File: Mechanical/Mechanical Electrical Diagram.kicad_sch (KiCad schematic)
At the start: 2 parts, among them U1 L298N

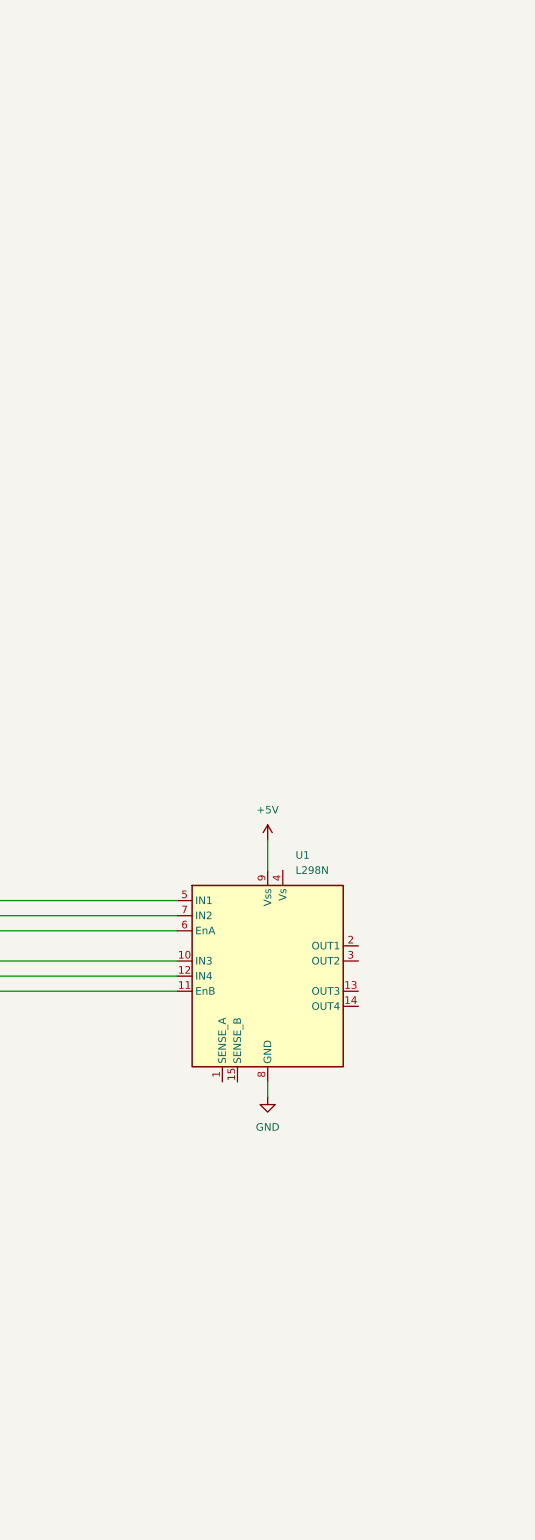
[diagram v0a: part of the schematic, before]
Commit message: Created Symbol Library
- Includes Jetson Nano
- Added Motor Controllers
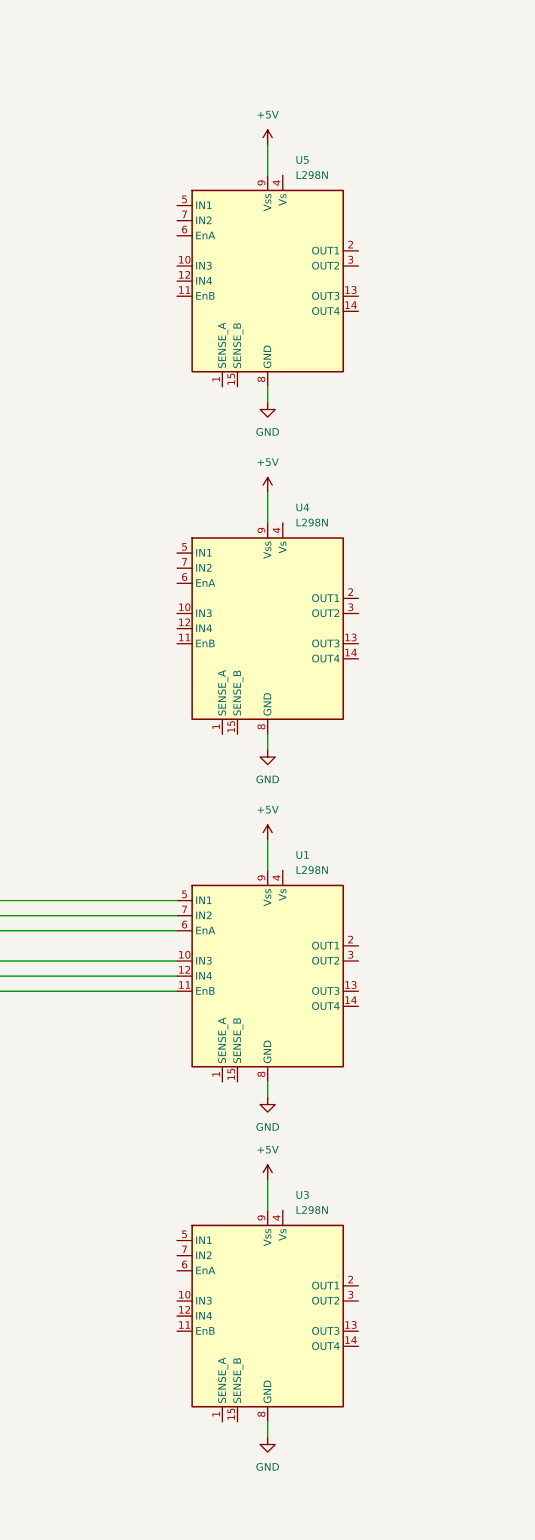
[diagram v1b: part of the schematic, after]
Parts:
- added U3, U4, U5: L298N, Package_TO_SOT_THT:TO-220-15_P2.54x5.08mm_StaggerOdd_Lead4.58mm_Vertical, symbol Driver_Motor:L298N
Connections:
- net +5V: now also U3.9 (Vss), U4.9 (Vss), U5.9 (Vss)
- net GND: now also U3.8 (GND), U4.8 (GND), U5.8 (GND)

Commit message: Updated Mechanical Wiring Diagram
- Removed Jetson Nano
- Added 4 Motor Controllers
- Added 4 Motors
- Waiting on Updated Symbol for Motors
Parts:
- removed U2: ~, symbol Jetson Nano:Jetson_Nano
- removed U4: L298N, Package_TO_SOT_THT:TO-220-15_P2.54x5.08mm_StaggerOdd_Lead4.58mm_Vertical, symbol Driver_Motor:L298N
- added M1, M2, M3, M4: Motor_DC, symbol Motor:Motor_DC
- added U2: L298N, Package_TO_SOT_THT:TO-220-15_P2.54x5.08mm_StaggerOdd_Lead4.58mm_Vertical, symbol Driver_Motor:L298N
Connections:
- net +5V: now also U2.9 (Vss)
- net GND: now also U2.8 (GND)
- net at U5.13 (OUT3): now also M1.1 (+)
- net at U5.14 (OUT4): now also M1.2 (-)
- net at U3.13 (OUT3): now also M4.1 (+)
- net at U3.14 (OUT4): now also M4.2 (-)
- net at U1.13 (OUT3): now also M2.1 (+)
- net at U1.14 (OUT4): now also M2.2 (-)
- new net: M3.1 (+), U2.13 (OUT3)
- new net: M3.2 (-), U2.14 (OUT4)
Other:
- moved on the sheet: U5

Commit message: Added notes to schematics
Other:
- note added: "Looks good, we'll just sub in the actual motor schematic from the library."
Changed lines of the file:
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@@
 	(generator_version "9.0")
 	(paper "A2")
+	(text "Looks good, we'll just sub in the actual motor schematic from the library. "
+		(exclude_from_sim no)
+		(at 206.756 218.694 0)
+		(effects
+			(font
+				(size 1.27 1.27)
+			)
+		)
+	)
 	(wire
 		(pts

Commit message: Fixed Sparkmax
I forgor that the encoder cable was separate from the white cable. Fixed it.
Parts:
- removed M1, M2, M3, M4: Motor_DC, symbol Motor:Motor_DC
- removed U1, U2, U3, U5: L298N, Package_TO_SOT_THT:TO-220-15_P2.54x5.08mm_StaggerOdd_Lead4.58mm_Vertical, symbol Driver_Motor:L298N
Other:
- note removed: "Looks good, we'll just sub in the actual motor schematic from the library."

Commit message: Updated Mechanical Diagram
Installed 5 Neo Motors and SparkMax Controllers
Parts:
- added U1, U10, U11, U12, U15, U17, U19, U2, U21, U3, U4, U5, U6, U7, U8, U9: ~, symbol Lunabotics 2025-26:Spark_Max_Motor_Controller
- added U13, U14, U16, U18, U20: ~, symbol Lunabotics 2025-26:Rev_Neo
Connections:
- new net: U11.1 (M+_(Red)), U19.1 (M+_(Red)), U6.1 (M+_(Red)), U7.1 (M+_(Red))
- new net: U11.2 (M-_(Black)), U18.1 (M+), U19.2 (M-_(Black)), U6.2 (M-_(Black)), U7.2 (M-_(Black))
- new net: U11.3 (Brushless_(White)), U18.3 (C), U19.3 (Brushless_(White)), U6.3 (Brushless_(White)), U7.3 (Brushless_(White))
- new net: U11.9 (Encoder_Sensor_(6Pin)), U18.4 (Enc_Cable), U19.9 (Encoder_Sensor_(6Pin)), U6.9 (Encoder_Sensor_(6Pin)), U7.9 (Encoder_Sensor_(6Pin))
- new net: U10.2 (M-_(Black)), U16.1 (M+), U17.2 (M-_(Black)), U4.2 (M-_(Black)), U5.2 (M-_(Black))
- new net: U10.3 (Brushless_(White)), U16.3 (C), U17.3 (Brushless_(White)), U4.3 (Brushless_(White)), U5.3 (Brushless_(White))
- new net: U10.9 (Encoder_Sensor_(6Pin)), U16.4 (Enc_Cable), U17.9 (Encoder_Sensor_(6Pin)), U4.9 (Encoder_Sensor_(6Pin)), U5.9 (Encoder_Sensor_(6Pin))
- new net: U14.1 (M+), U15.2 (M-_(Black)), U2.2 (M-_(Black)), U3.2 (M-_(Black)), U9.2 (M-_(Black))
- new net: U14.3 (C), U15.3 (Brushless_(White)), U2.3 (Brushless_(White)), U3.3 (Brushless_(White)), U9.3 (Brushless_(White))
- new net: U14.4 (Enc_Cable), U15.9 (Encoder_Sensor_(6Pin)), U2.9 (Encoder_Sensor_(6Pin)), U3.9 (Encoder_Sensor_(6Pin)), U9.9 (Encoder_Sensor_(6Pin))
- new net: U15.1 (M+_(Red)), U2.1 (M+_(Red)), U3.1 (M+_(Red)), U9.1 (M+_(Red))
- new net: U12.1 (M+_(Red)), U21.1 (M+_(Red)), U8.1 (M+_(Red))
- new net: U12.2 (M-_(Black)), U20.1 (M+), U21.2 (M-_(Black)), U8.2 (M-_(Black))
- new net: U12.3 (Brushless_(White)), U20.3 (C), U21.3 (Brushless_(White)), U8.3 (Brushless_(White))
- new net: U12.9 (Encoder_Sensor_(6Pin)), U20.4 (Enc_Cable), U21.9 (Encoder_Sensor_(6Pin)), U8.9 (Encoder_Sensor_(6Pin))
- new net: U10.1 (M+_(Red)), U17.1 (M+_(Red)), U4.1 (M+_(Red)), U5.1 (M+_(Red))
- new net: U1.2 (M-_(Black)), U13.1 (M+)
- new net: U1.3 (Brushless_(White)), U13.3 (C)
- new net: U1.9 (Encoder_Sensor_(6Pin)), U13.4 (Enc_Cable)
- new net +12V: U1.4 (V+), U10.4 (V+), U11.4 (V+), U12.4 (V+), U15.4 (V+), U17.4 (V+), U19.4 (V+), U2.4 (V+), U21.4 (V+), U3.4 (V+), U4.4 (V+), U5.4 (V+), U6.4 (V+), U7.4 (V+), U8.4 (V+), U9.4 (V+)
- new net GND: U1.5 (V-), U10.5 (V-), U11.5 (V-), U12.5 (V-), U15.5 (V-), U17.5 (V-), U19.5 (V-), U2.5 (V-), U21.5 (V-), U3.5 (V-), U4.5 (V-), U5.5 (V-), U6.5 (V-), U7.5 (V-), U8.5 (V-), U9.5 (V-)
